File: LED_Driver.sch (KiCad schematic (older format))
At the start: 6 parts, among them U2 AP5726

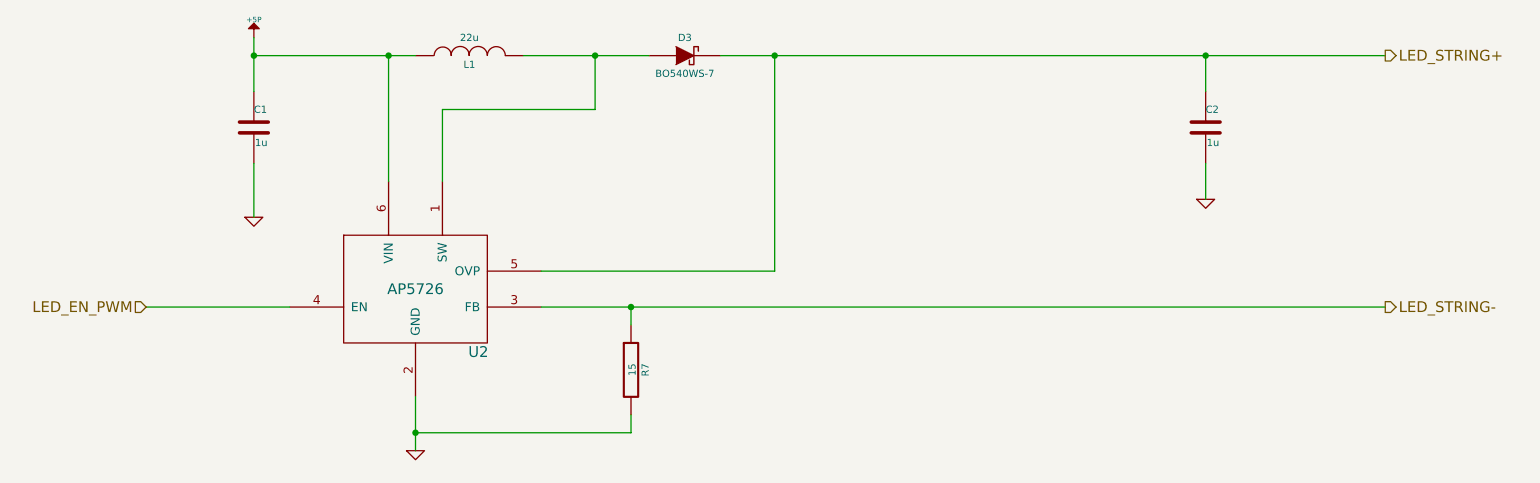
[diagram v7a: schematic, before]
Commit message: Updates from Layout Work Session 4 video
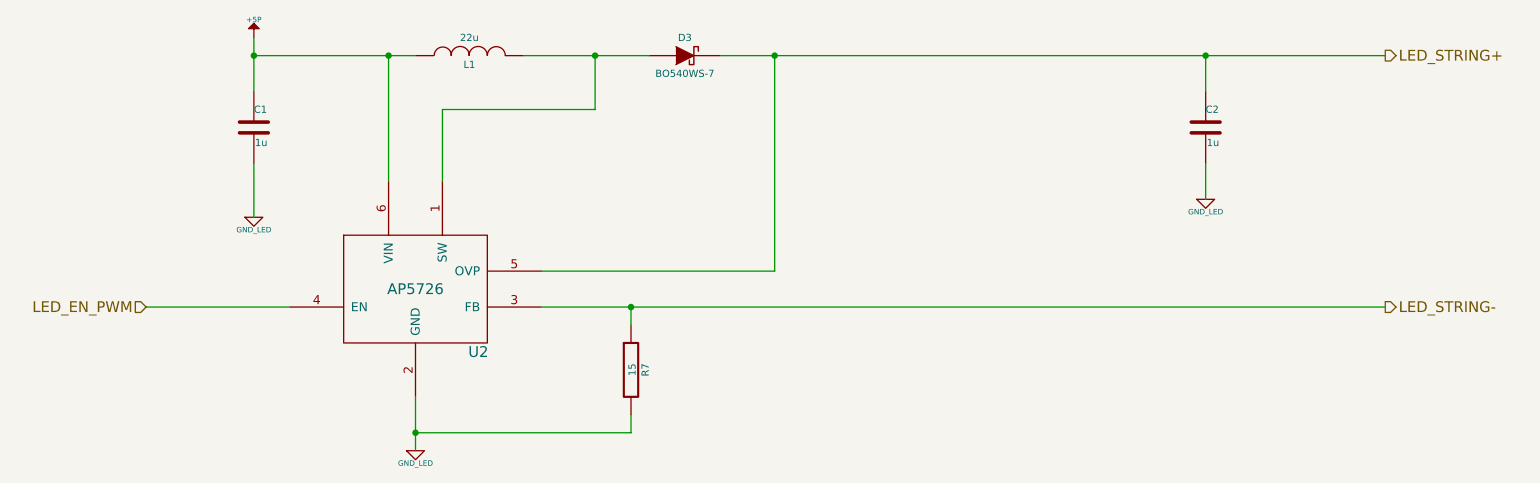
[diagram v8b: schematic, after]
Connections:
- net GND renamed GND_LED
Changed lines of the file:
@@
-	1    0    0    -1
-$EndComp
-$Comp
-L GND #PWR03
-U 1 1 52F2BDE9
-P 3200 1900
-F 0 "#PWR03" H 3200 1900 30  0001 C CNN
-F 1 "GND" H 3200 1830 30  0001 C CNN
-F 2 "" H 3200 1900 60  0000 C CNN
-F 3 "" H 3200 1900 60  0000 C CNN
-	1    3200 1900
-	1    0    0    -1
-$EndComp
-$Comp
-L GND #PWR04
-U 1 1 52F2BDFB
-P 4100 3200
-F 0 "#PWR04" H 4100 3200 30  0001 C CNN
-F 1 "GND" H 4100 3130 30  0001 C CNN
-F 2 "" H 4100 3200 60  0000 C CNN
-F 3 "" H 4100 3200 60  0000 C CNN
-	1    4100 3200
 	1    0    0    -1
 $EndComp
@@
 Wire Wire Line
 	8500 1000 8500 1200
-$Comp
-L GND #PWR05
-U 1 1 52F2BEC8
-P 8500 1800
-F 0 "#PWR05" H 8500 1800 30  0001 C CNN
-F 1 "GND" H 8500 1730 30  0001 C CNN
-F 2 "" H 8500 1800 60  0000 C CNN
-F 3 "" H 8500 1800 60  0000 C CNN
-	1    8500 1800
-	1    0    0    -1
-$EndComp
 Wire Wire Line
 	8500 1800 8500 1600
@@
 	1    0    0    -1
 $EndComp
+$Comp
+L GND_LED #PWR03
+U 1 1 5315244B
+P 4100 3200
+F 0 "#PWR03" H 4100 3200 30  0001 C CNN
+F 1 "GND_LED" H 4100 3130 30  0000 C CNN
+F 2 "" H 4100 3200 60  0000 C CNN
+F 3 "" H 4100 3200 60  0000 C CNN
+	1    4100 3200
+	1    0    0    -1
+$EndComp
+$Comp
+L GND_LED #PWR04
+U 1 1 5315245D
+P 8500 1800
+F 0 "#PWR04" H 8500 1800 30  0001 C CNN
+F 1 "GND_LED" H 8500 1730 30  0000 C CNN
+F 2 "" H 8500 1800 60  0000 C CNN
+F 3 "" H 8500 1800 60  0000 C CNN
+	1    8500 1800
+	1    0    0    -1
+$EndComp
+$Comp
+L GND_LED #PWR05
+U 1 1 53152468
+P 3200 1900
+F 0 "#PWR05" H 3200 1900 30  0001 C CNN
+F 1 "GND_LED" H 3200 1830 30  0000 C CNN
+F 2 "" H 3200 1900 60  0000 C CNN
+F 3 "" H 3200 1900 60  0000 C CNN
+	1    3200 1900
+	1    0    0    -1
+$EndComp
